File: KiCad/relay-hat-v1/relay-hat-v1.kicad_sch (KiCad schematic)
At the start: 50 parts, among them J1 Screw_Terminal_01x04, J2 Conn_01x04_Pin, M1 Fan, U1 TCA9554PW, U10 TMP1075DGKR, U11 LM311, U12 TPS2051CDBV, U2 TPS2051CDBV, U3 TPS2051CDBV, U4 TPS2051CDBV, U5 TPS2051CDBV, U6 TPS2051CDBV, U7 TPS2000CDGK, U8 TPS2000CDGK, U9 TPS2000CDGK

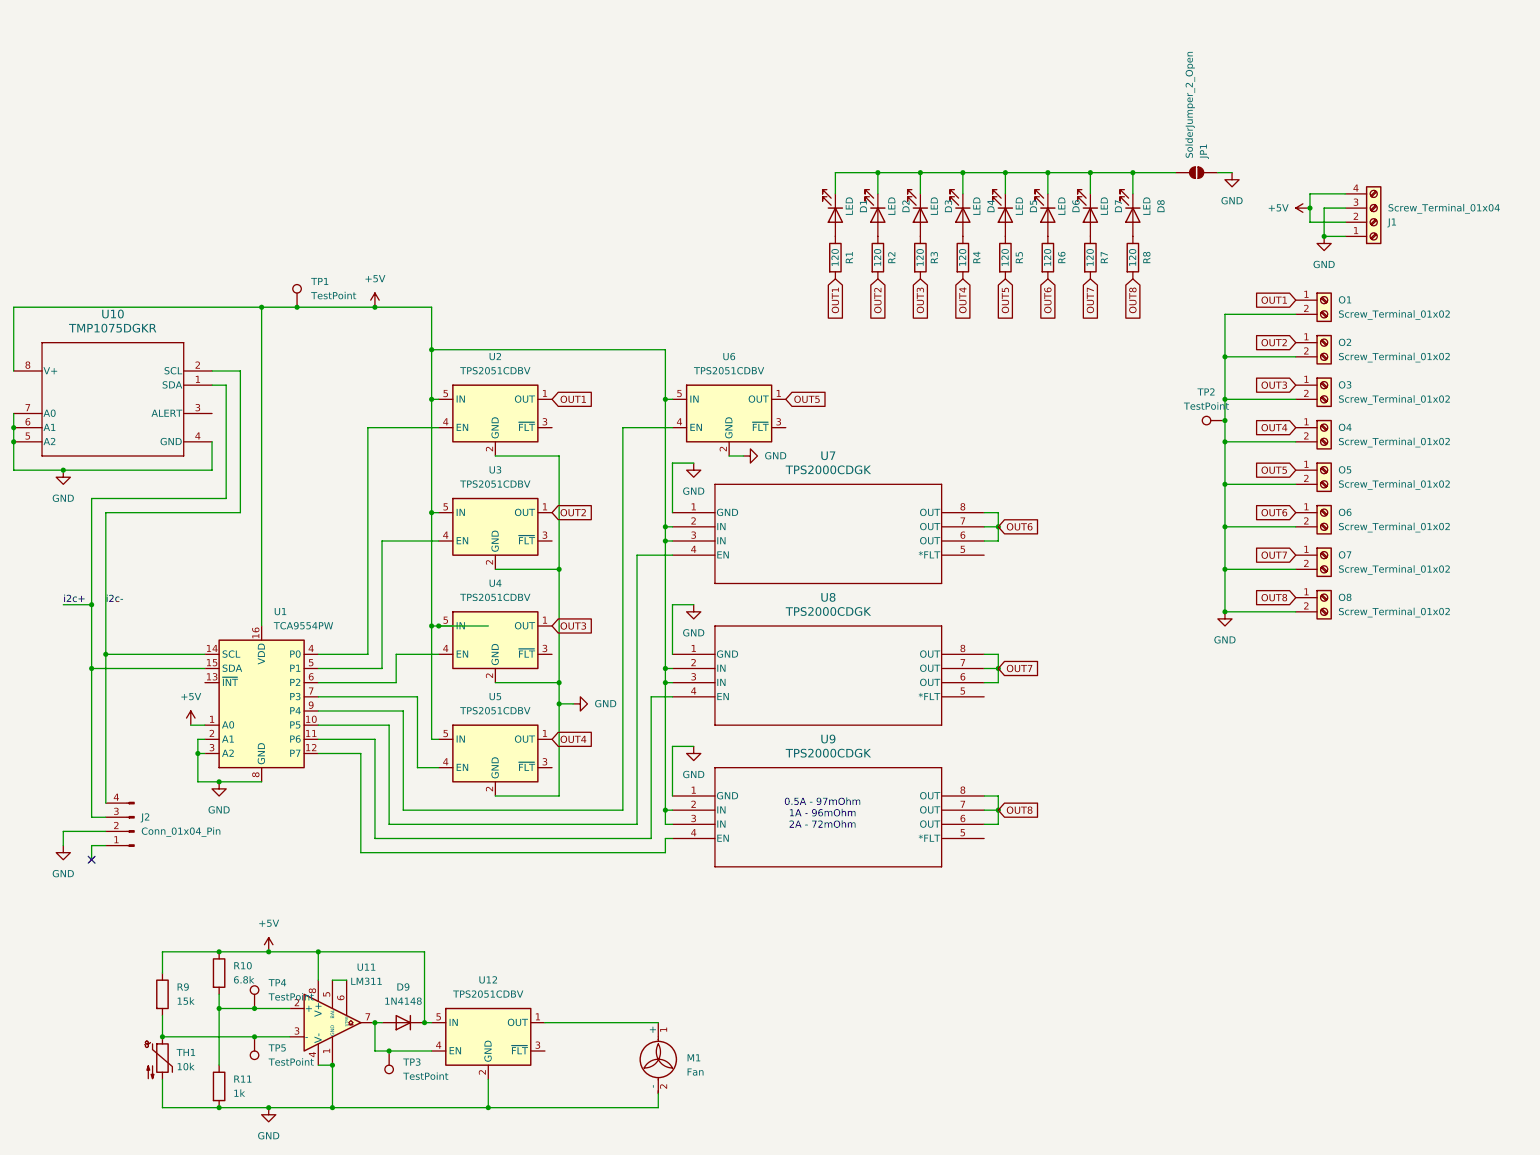
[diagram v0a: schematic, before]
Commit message: Test code and changed diode for resistor
The diode after the op-amp on the relay board is now a 10K pullup resistor
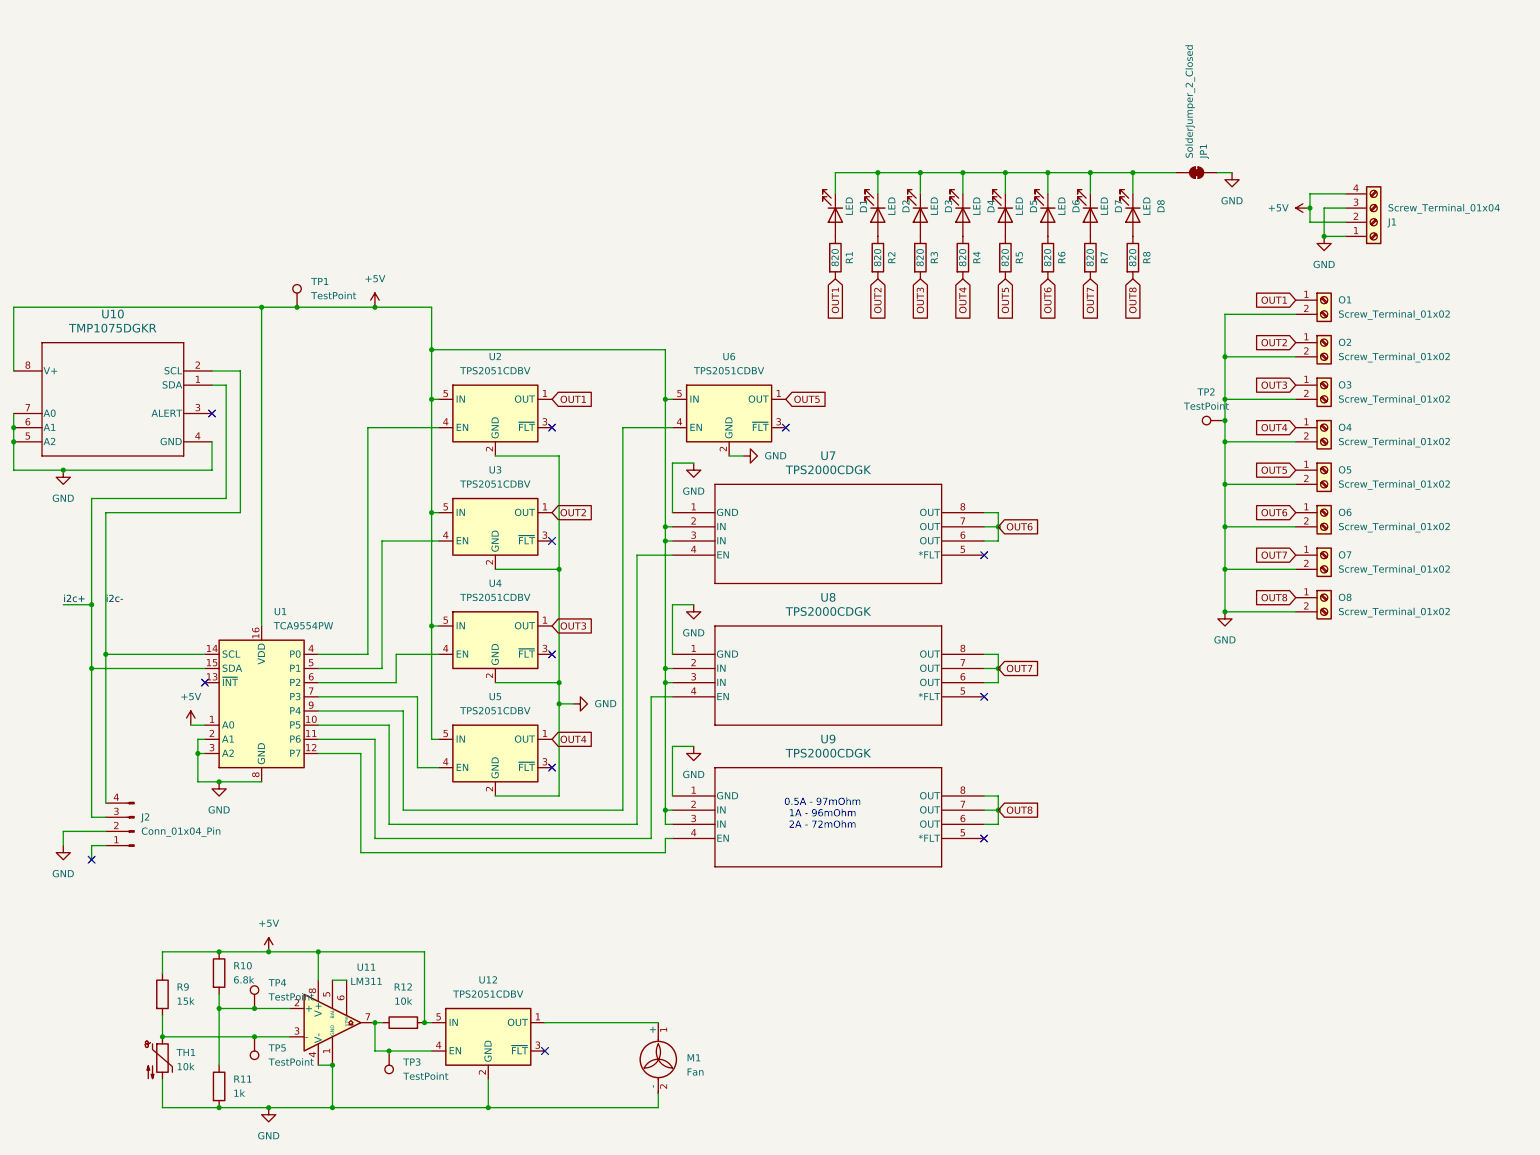
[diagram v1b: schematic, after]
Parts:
- removed D9: 1N4148, Diode_SMD:D_SOD-123, symbol Diode:1N4148
- added R12: 10k, Resistor_SMD:R_0805_2012Metric_Pad1.20x1.40mm_HandSolder, symbol Device:R
- JP1: value SolderJumper_2_Open -> SolderJumper_2_Closed; symbol Jumper:SolderJumper_2_Open -> Jumper:SolderJumper_2_Bridged
- R1, R2, R3, R4, R5, R6, R7, R8: value 120 -> 820
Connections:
- net +5V: now also R12.2
- net at TP3.1, U11.7, U12.4 (EN): now also R12.1
- no-connect marks 1 -> 12
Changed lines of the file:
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@@
 	)
 	(junction
-		(at 118.11 106.68)
+		(at 93.98 167.64)
 		(diameter 0)
 		(color 0 0 0 0)
 	)
 	(junction
-		(at 137.16 129.54)
+		(at 118.11 106.68)
 		(diameter 0)
 		(color 0 0 0 0)
 	)
 	(junction
-		(at 57.15 124.46)
+		(at 137.16 129.54)
 		(diameter 0)
 		(color 0 0 0 0)
 	)
 	(junction
-		(at 93.98 167.64)
+		(at 57.15 124.46)
 		(diameter 0)
 		(color 0 0 0 0)
@@
 		(color 0 0 0 0)
 	)
-	(junction
-		(at 96.52 96.52)
-		(diameter 0)
-		(color 0 0 0 0)
+	(no_connect
+		(at 115.57 172.72)
+	)
+	(no_connect
+		(at 194.31 109.22)
+	)
+	(no_connect
+		(at 55.88 58.42)
 	)
 	(no_connect
 		(at 34.29 138.43)
 	)
+	(no_connect
+		(at 158.75 60.96)
+	)
+	(no_connect
+		(at 116.84 60.96)
+	)
+	(no_connect
+		(at 194.31 83.82)
+	)
+	(no_connect
+		(at 194.31 134.62)
+	)
+	(no_connect
+		(at 116.84 121.92)
+	)
+	(no_connect
+		(at 54.61 106.68)
+	)
+	(no_connect
+		(at 116.84 101.6)
+	)
+	(no_connect
+		(at 116.84 81.28)
+	)
 	(wire
 		(pts
@@
 	(wire
 		(pts
-			(xy 96.52 96.52) (xy 105.41 96.52)
-		)
-		(stroke
-			(width 0)
-			(type default)
-		)
-	)
-	(wire
-		(pts
 			(xy 36.83 135.89) (xy 34.29 135.89)
 		)
@@
 			)
 		)
-		(property "Value" "120"
+		(property "Value" "820"
 			(at 213.36 30.48 90)
 			(effects
@@
 			)
 		)
-		(property "Value" "120"
+		(property "Value" "820"
 			(at 205.74 30.48 90)
 			(effects
@@
 			)
 		)
-		(property "Value" "120"
+		(property "Value" "820"
 			(at 175.26 30.48 90)
 			(effects
@@
 			)
 		)
-		(property "Value" "120"
+		(property "Value" "820"
 			(at 198.12 30.48 90)
 			(effects
@@
 	)
 	(symbol
-		(lib_id "Jumper:SolderJumper_2_Open")
+		(lib_id "Jumper:SolderJumper_2_Bridged")
 		(at 232.41 15.24 0)
 		(mirror x)
@@
 			)
 		)
-		(property "Value" "SolderJumper_2_Open"
+		(property "Value" "SolderJumper_2_Closed"
 			(at 231.1401 12.7 90)
 			(effects
@@
 			)
 		)
-		(property "Description" "Solder Jumper, 2-pole, open"
+		(property "Description" "Solder Jumper, 2-pole, closed/bridged"
 			(at 232.41 15.24 0)
 			(effects
@@
 			)
 		)
-		(property "Value" "120"
+		(property "Value" "820"
 			(at 190.5 30.48 90)
 			(effects
@@
 			)
 		)
-		(property "Value" "120"
+		(property "Value" "820"
 			(at 182.88 30.48 90)
 			(effects
@@
 	)
 	(symbol
-		(lib_id "Diode:1N4148")
-		(at 90.17 167.64 180)
+		(lib_id "Device:R")
+		(at 90.17 167.64 90)
 		(unit 1)
 		(exclude_from_sim no)
@@
 		(dnp no)
 		(fields_autoplaced yes)
-		(property "Reference" "D9"
-			(at 90.17 161.29 0)
-			(effects
-				(font
-					(size 1.27 1.27)
-				)
-			)
-		)
-		(property "Value" "1N4148"
-			(at 90.17 163.83 0)
+		(property "Reference" "R12"
+			(at 90.17 161.29 90)
 			(effects
 				(font
@@
 			)
 		)
-		(property "Footprint" "Diode_SMD:D_SOD-123"
-			(at 90.17 167.64 0)
-			(effects
-				(font
-					(size 1.27 1.27)
-				)
-				(hide yes)
-			)
-		)
-		(property "Datasheet" "https://assets.nexperia.com/documents/data-sheet/1N4148_1N4448.pdf"
-			(at 90.17 167.64 0)
+		(property "Value" "10k"
+			(at 90.17 163.83 90)
 			(effects
 				(font
 					(size 1.27 1.27)
 				)
-				(hide yes)
 			)
 		)
-		(property "Description" "100V 0.15A standard switching diode, DO-35"
-			(at 90.17 167.64 0)
+		(property "Footprint" "Resistor_SMD:R_0805_2012Metric_Pad1.20x1.40mm_HandSolder"
+			(at 90.17 169.418 90)
 			(effects
 				(font
@@
 			)
 		)
-		(property "Sim.Device" "D"
+		(property "Datasheet" "~"
 			(at 90.17 167.64 0)
 			(effects
@@
 			)
 		)
-		(property "Sim.Pins" "1=K 2=A"
+		(property "Description" "Resistor"
 			(at 90.17 167.64 0)
 			(effects
@@
 			(project "relay-hat-v1"
 				(path "/34d803bb-2b43-40ec-9a9e-8066d156d755"
-					(reference "D9")
+					(reference "R12")
 					(unit 1)
 				)
@@
 			)
 		)
-		(property "Value" "120"
+		(property "Value" "820"
 			(at 220.98 30.48 90)
 			(effects
@@
 			)
 		)
-		(property "Value" "120"
+		(property "Value" "820"
 			(at 167.64 30.48 90)
 			(effects

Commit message: Updated some code and micro-some-brero
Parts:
- U7, U8, U9: value TPS2000CDGK -> TPS2001CDGK
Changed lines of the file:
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@@
 			)
 		)
-		(property "Value" "TPS2000CDGK"
+		(property "Value" "TPS2001CDGK"
 			(at 166.37 68.58 0)
 			(effects
@@
 			)
 		)
-		(property "Value" "TPS2000CDGK"
+		(property "Value" "TPS2001CDGK"
 			(at 166.37 119.38 0)
 			(effects
@@
 			)
 		)
-		(property "Value" "TPS2000CDGK"
+		(property "Value" "TPS2001CDGK"
 			(at 166.37 93.98 0)
 			(effects
